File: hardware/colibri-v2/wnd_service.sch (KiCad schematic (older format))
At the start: 31 parts

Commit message: work on cortex sheet.
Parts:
- removed R?: 1k2/5%, Resistors_SMD:R_0603, symbol R_SMT
- added R?: 360R, Resistors_SMD:R_0603, symbol R_SMT
- R?: value 620R/5% -> 750R; Part 2141352 -> 9331506
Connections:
- net +3V3: now also R?.1
- net at DL?.2 (A): now also R?.2
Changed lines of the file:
@@
-$EndComp
-$Comp
-L R_SMT R?
-U 1 1 56AB2378
-P 10150 2750
-F 0 "R?" V 10220 2750 50  0000 C CNN
-F 1 "1k2/5%" V 10080 2750 50  0000 C CNN
-F 2 "Resistors_SMD:R_0603" V 10300 2750 30  0001 C CNN
-F 3 "" V 10230 2750 30  0000 C CNN
-F 4 "0603" V 10150 2750 20  0000 C CNN "SMT"
-F 5 "9331751" V 10350 2750 30  0001 C CNN "Part"
-F 6 "Farnell" V 10400 2750 30  0001 C CNN "Provider"
-	1    10150 2750
-	-1   0    0    1
 $EndComp
 $Comp
@@
 P 10150 4850
 F 0 "R?" H 10200 5000 50  0000 C CNN
-F 1 "620R/5%" V 10080 4850 50  0000 C CNN
+F 1 "750R" V 10080 4850 50  0000 C CNN
 F 2 "Resistors_SMD:R_0603" V 10300 4850 30  0001 C CNN
 F 3 "" V 10230 4850 30  0000 C CNN
 F 4 "0603" V 10150 4850 20  0000 C CNN "SMT"
-F 5 "2141352" V 10350 4850 30  0001 C CNN "Part"
+F 5 "9331506" V 10350 4850 30  0001 C CNN "Part"
 F 6 "Farnell" V 10400 4850 30  0001 C CNN "Provider"
 	1    10150 4850
@@
 Wire Wire Line
 	2950 5050 3700 5050
+$Comp
+L R_SMT R?
+U 1 1 56AD7549
+P 10150 2750
+F 0 "R?" H 10200 2900 50  0000 C CNN
+F 1 "360R" V 10080 2750 50  0000 C CNN
+F 2 "Resistors_SMD:R_0603" V 10300 2750 30  0001 C CNN
+F 3 "" V 10230 2750 30  0000 C CNN
+F 4 "0603" V 10150 2750 20  0000 C CNN "SMT"
+F 5 "9331077" V 10350 2750 30  0001 C CNN "Part"
+F 6 "Farnell" V 10400 2750 30  0001 C CNN "Provider"
+	1    10150 2750
+	1    0    0    -1
+$EndComp
 $EndSCHEMATC

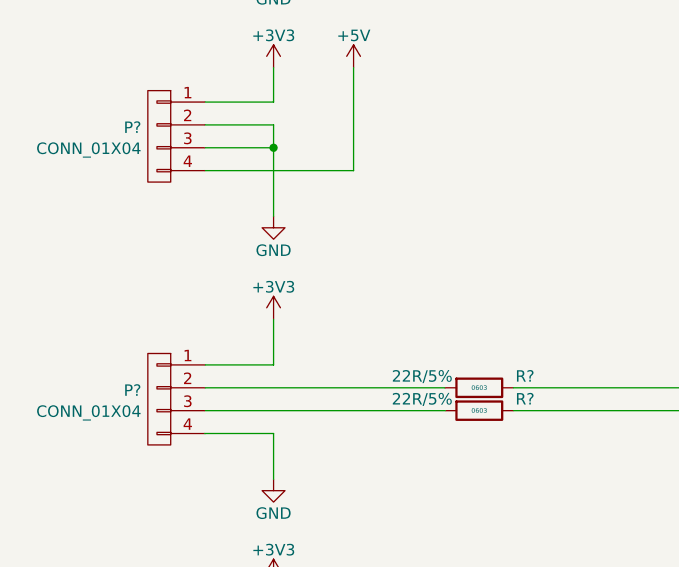
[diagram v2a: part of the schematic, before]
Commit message: Added ext_sensors.sch sheet
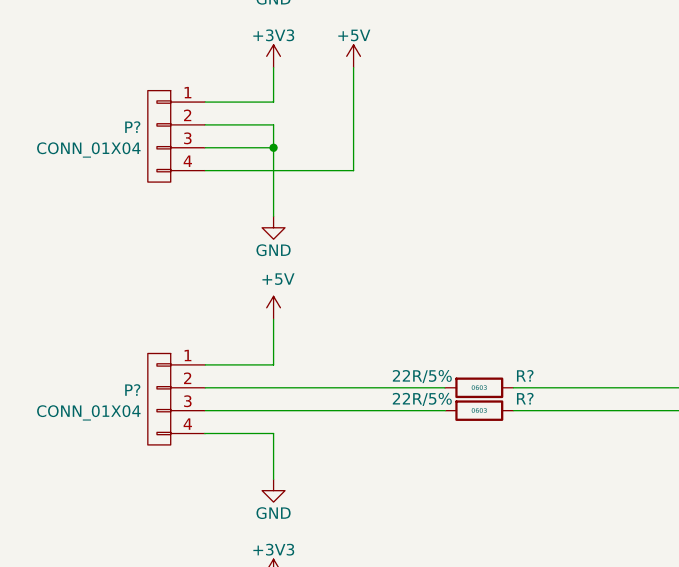
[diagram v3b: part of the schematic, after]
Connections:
- net +3V3: no longer P?.1 (P1)
- net +5V: now also P?.1 (P1)
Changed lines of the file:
@@
 Wire Wire Line
 	1900 1050 1900 850
-$Comp
-L +3V3 #PWR?
-U 1 1 56AC8575
-P 1900 3500
-F 0 "#PWR?" H 1900 3350 50  0001 C CNN
-F 1 "+3V3" H 1900 3640 50  0000 C CNN
-F 2 "" H 1900 3500 60  0000 C CNN
-F 3 "" H 1900 3500 60  0000 C CNN
-	1    1900 3500
-	1    0    0    -1
-$EndComp
 Wire Wire Line
 	1600 3700 1900 3700
@@
 	1    0    0    -1
 $EndComp
+$Comp
+L +5V #PWR?
+U 1 1 56CC4D65
+P 1900 3500
+F 0 "#PWR?" H 1900 3350 50  0001 C CNN
+F 1 "+5V" H 1918 3674 50  0000 C CNN
+F 2 "" H 1900 3500 50  0000 C CNN
+F 3 "" H 1900 3500 50  0000 C CNN
+	1    1900 3500
+	1    0    0    -1
+$EndComp

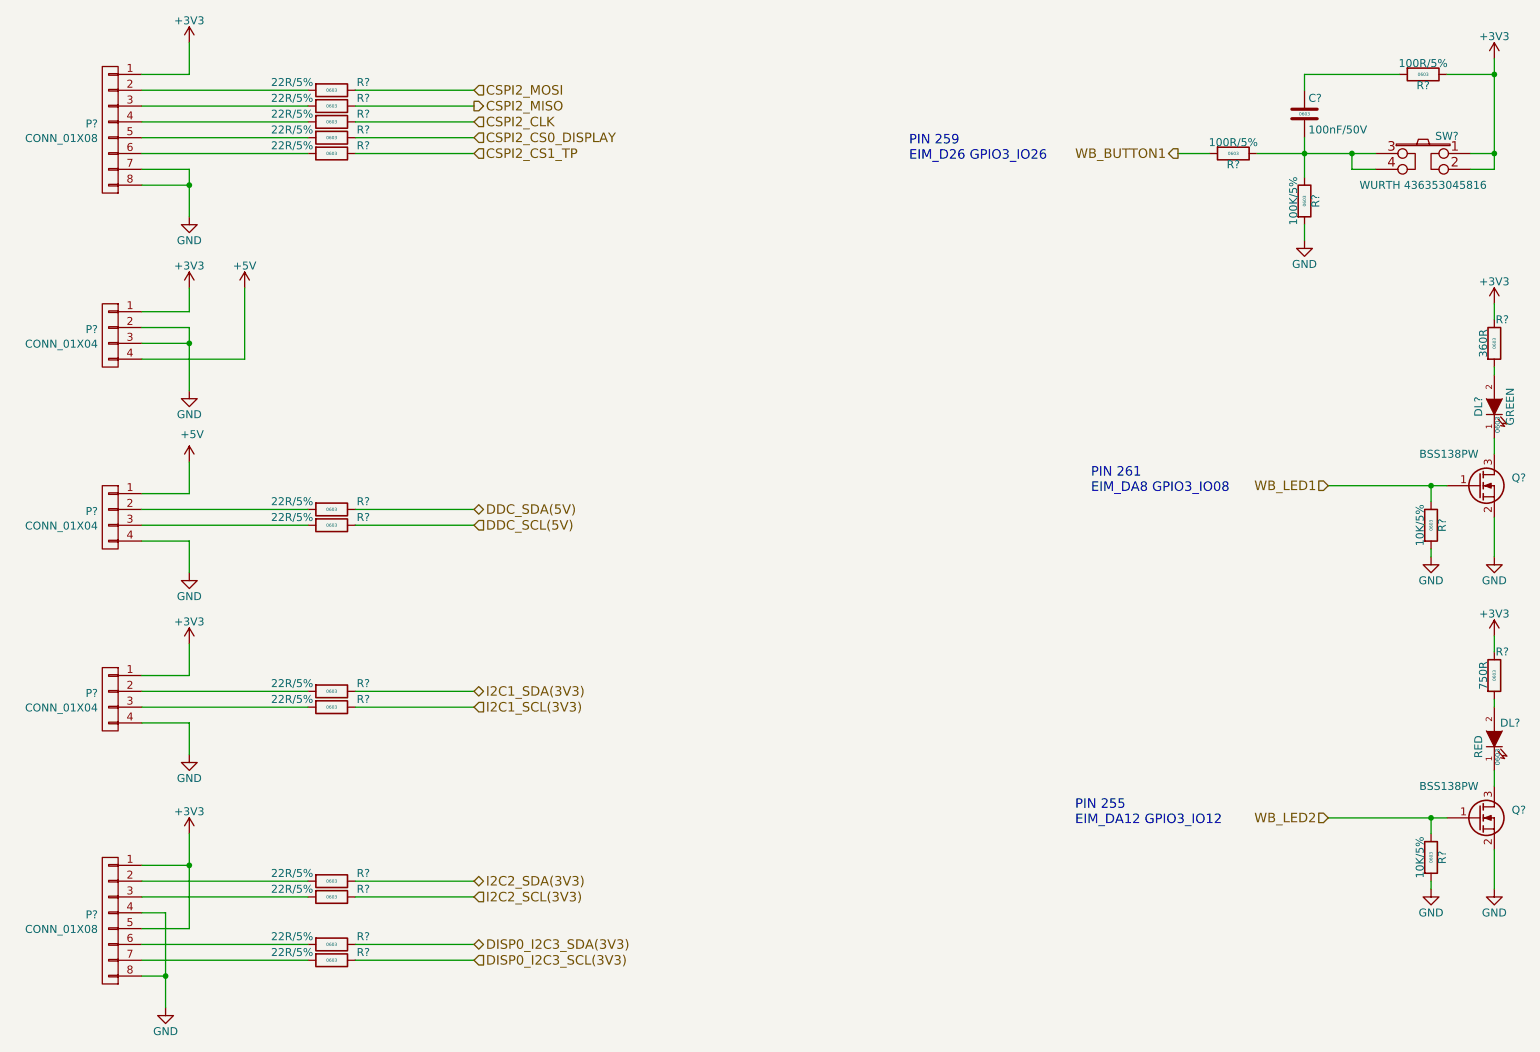
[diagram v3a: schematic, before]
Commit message: Resolving ERC problems
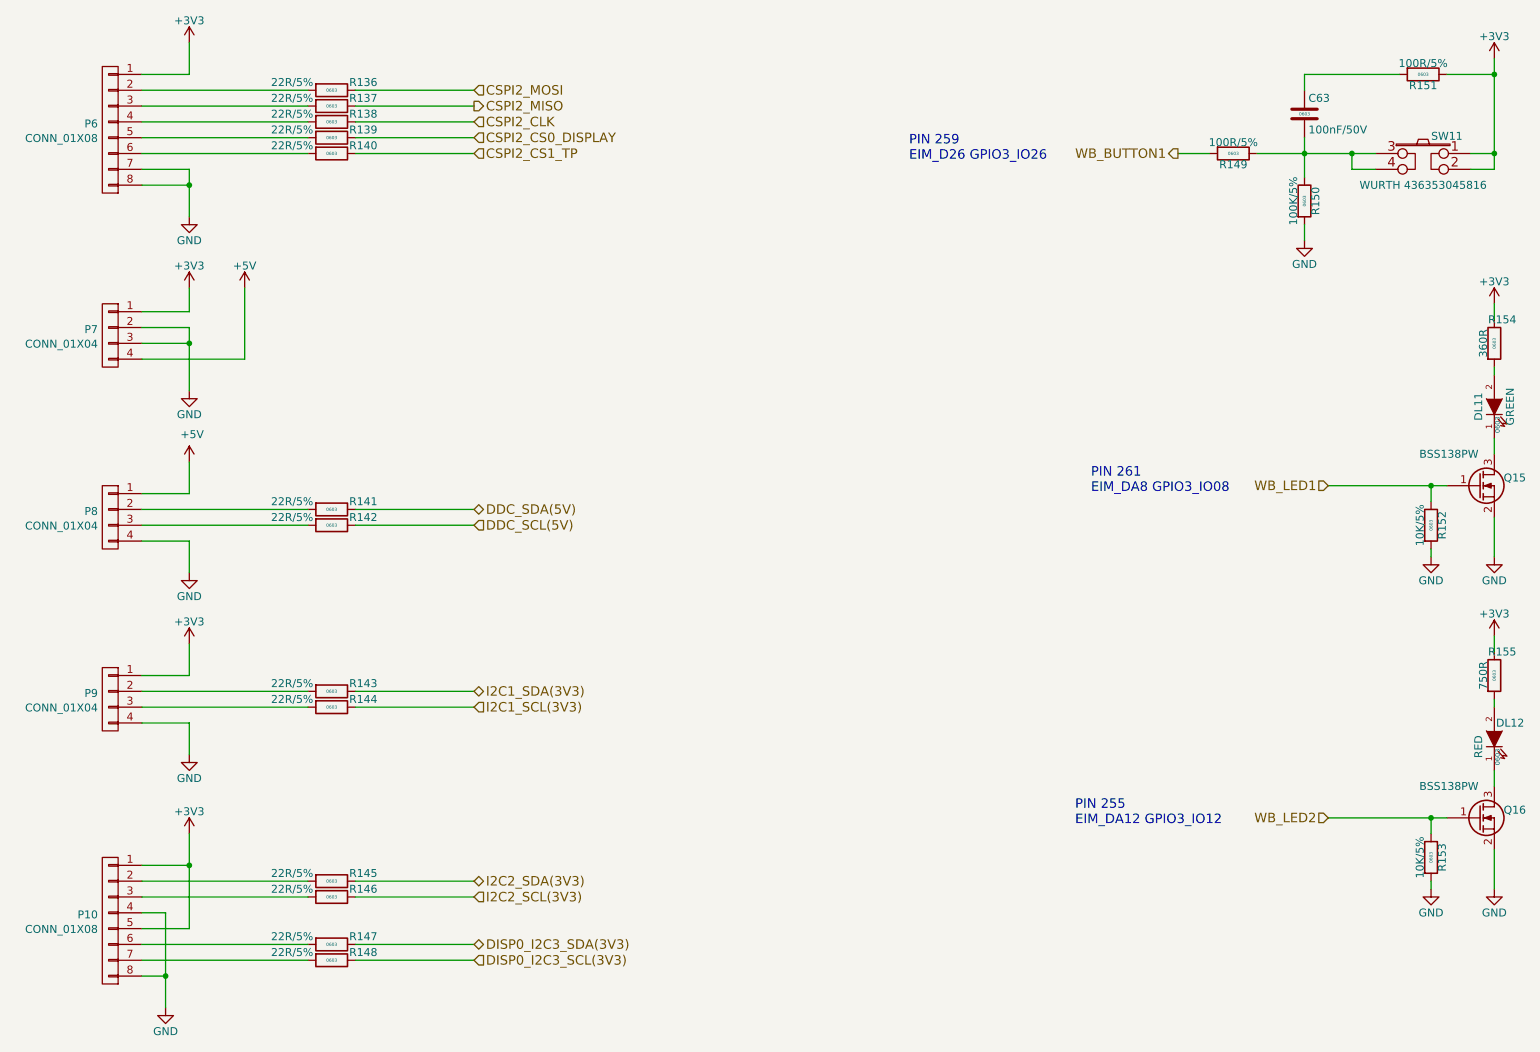
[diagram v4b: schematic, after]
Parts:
- gave numbers to parts that had none: 31
